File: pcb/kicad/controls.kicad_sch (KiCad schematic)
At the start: 0 parts

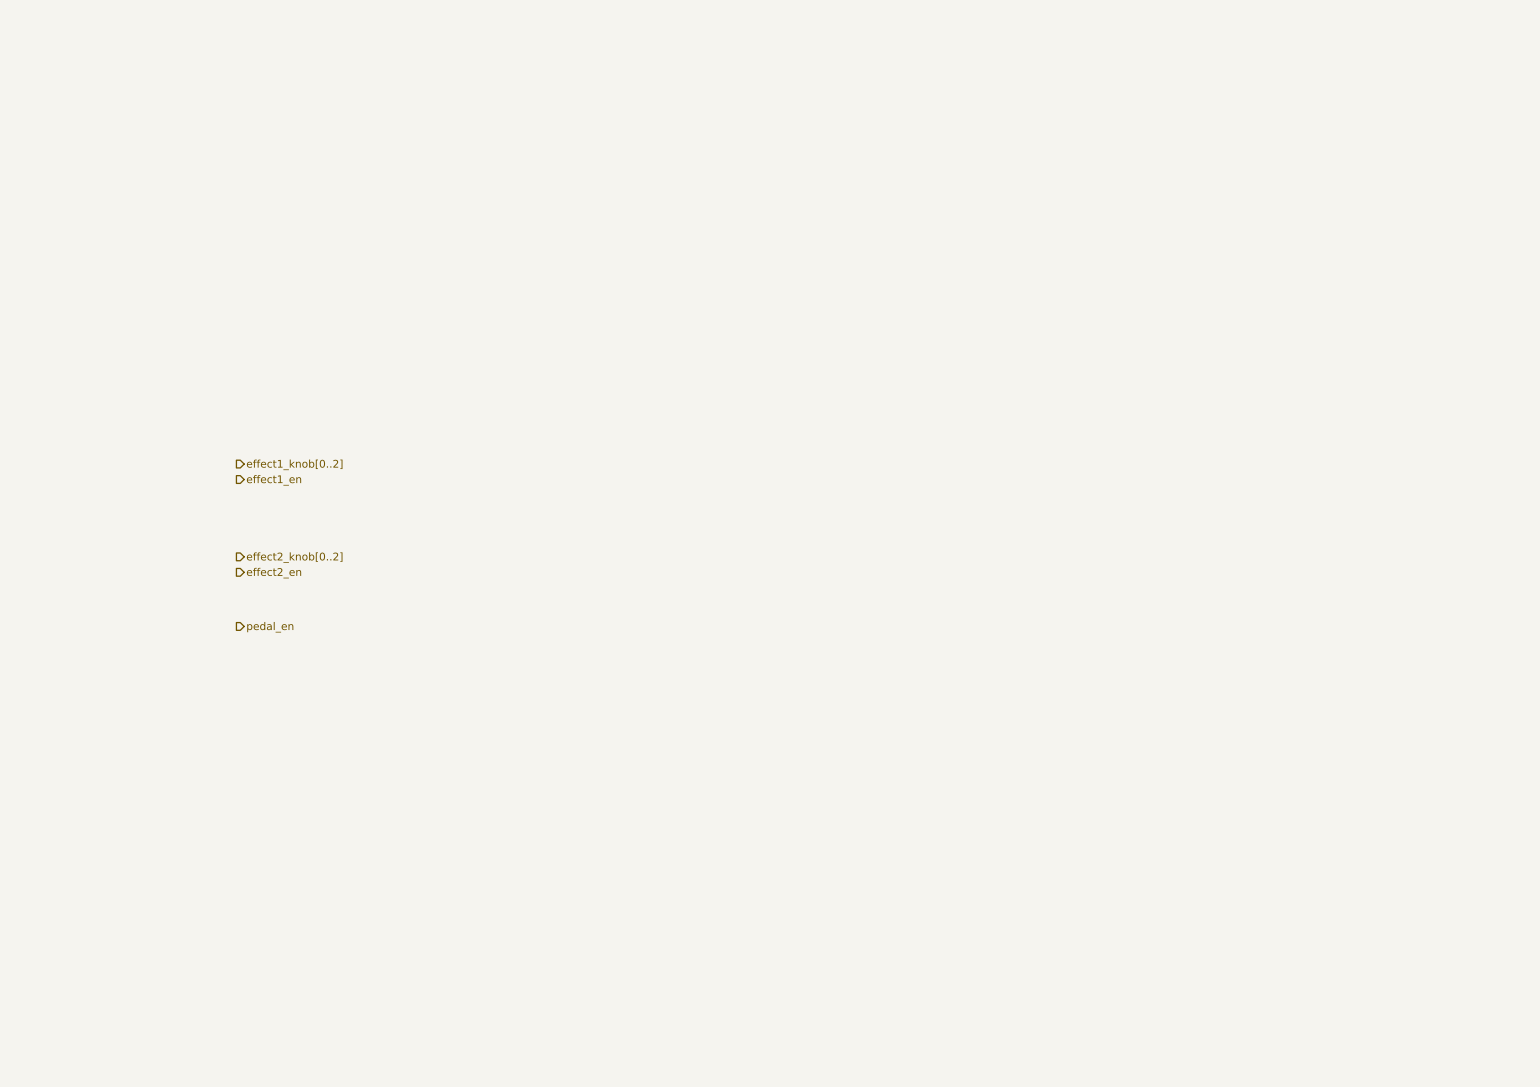
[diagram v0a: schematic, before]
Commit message: Added converters, controls and updated annotations.
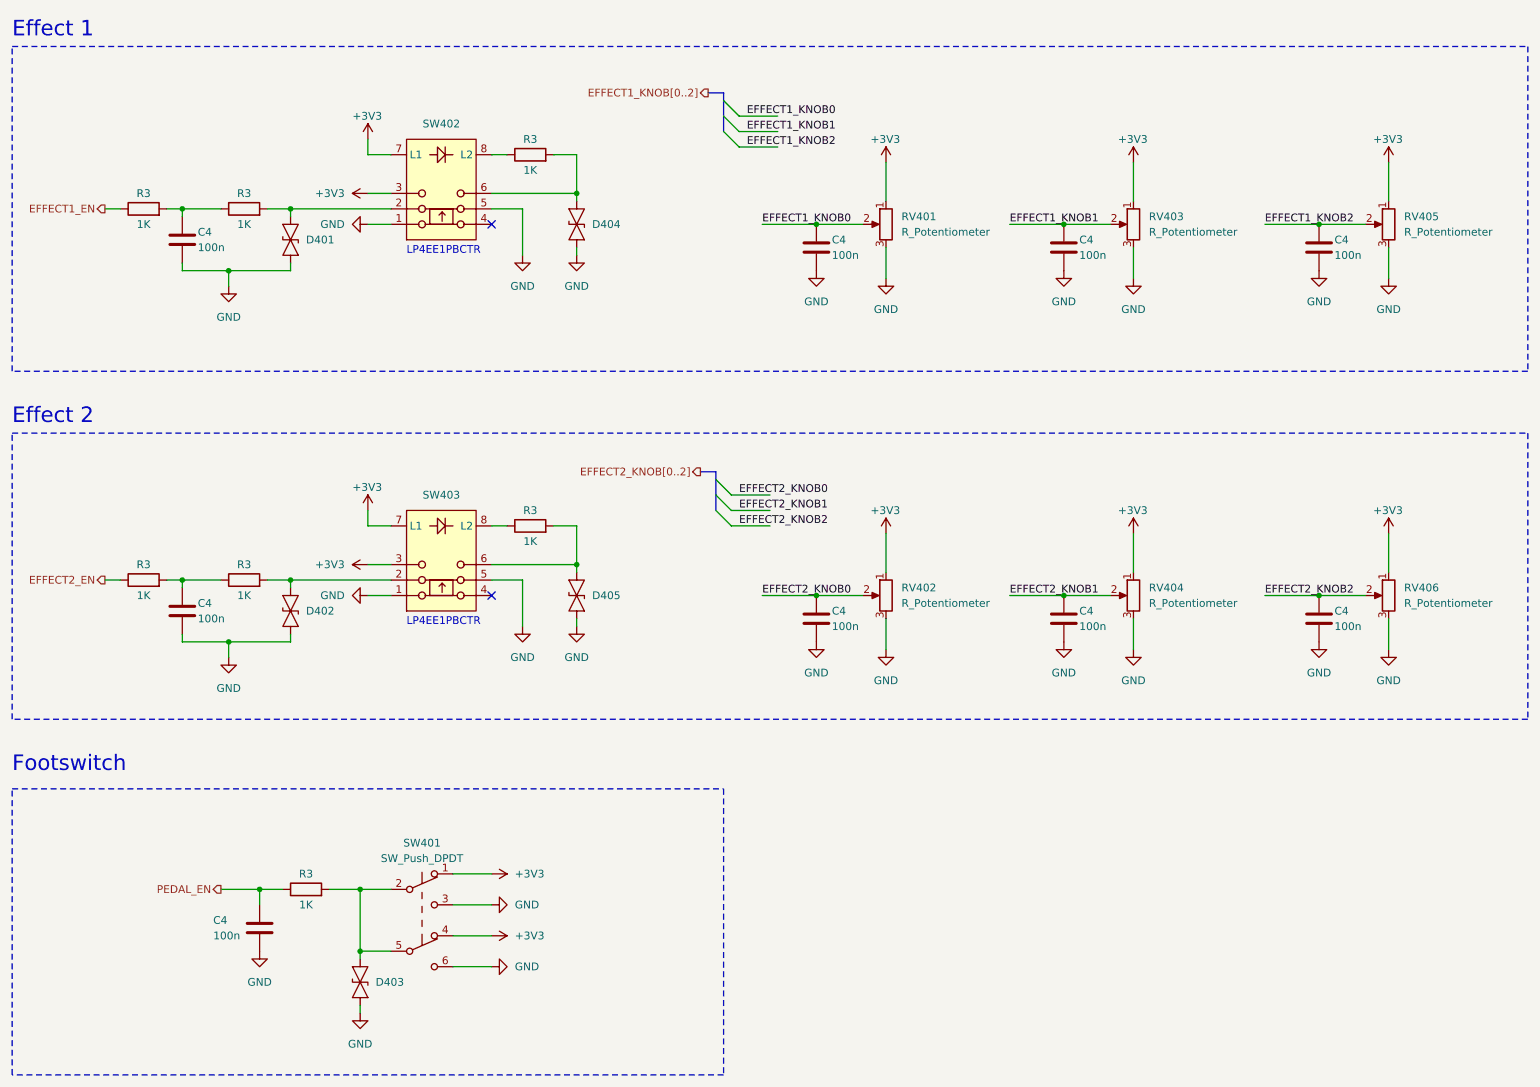
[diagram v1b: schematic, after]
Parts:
- added C4 (x9): 100n, Capacitor_SMD:C_0805_2012Metric, symbol Device:C
- added D401, D402, D403, D404, D405: ~, symbol pedal-components:PESD3V3L1BA
- added R3 (x7): 1K, Resistor_SMD:R_0805_2012Metric, symbol Device:R
- added RV401, RV402, RV403, RV404, RV405, RV406: R_Potentiometer, symbol Device:R_Potentiometer
- added SW401: SW_Push_DPDT, symbol Switch:SW_Push_DPDT
- added SW402, SW403: ~, symbol pedal-components:LP4EE1PBCTR
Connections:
- new net: D404.1 (A1), R3.2, SW402.6
- new net: C4.1, R3.1, R3.2 (x2)
- new net: D401.2 (A2), R3.2, SW402.2
- new net: R3.1, SW402.8 (L2)
- new net: D403.2 (A2), R3.2, SW401.2 (B), SW401.5 (B)
- new net: R3.1, SW403.8 (L2)
- new net: D405.1 (A1), R3.2, SW403.6
- new net: D402.2 (A2), R3.2, SW403.2
- new net +3V3: RV401.1, RV402.1, RV403.1, RV404.1, RV405.1, RV406.1, SW401.1 (A), SW401.4 (A), SW402.3, SW402.7 (L1), SW403.3, SW403.7 (L1)
- new net EFFECT1_EN: R3.1
- new net EFFECT1_KNOB0: C4.1, RV401.2
- new net EFFECT1_KNOB1: C4.1, RV403.2
- new net EFFECT1_KNOB2: C4.1, RV405.2
- new net EFFECT2_EN: R3.1
- new net EFFECT2_KNOB0: C4.1, RV402.2
- new net EFFECT2_KNOB1: C4.1, RV404.2
- new net EFFECT2_KNOB2: C4.1, RV406.2
- new net GND: C4.2, C4.2, C4.2, C4.2, C4.2, C4.2, C4.2, C4.2, C4.2, D401.1 (A1), D402.1 (A1), D403.1 (A1), D404.2 (A2), D405.2 (A2), RV401.3, RV402.3, RV403.3, RV404.3, RV405.3, RV406.3, SW401.3 (C), SW401.6 (C), SW402.1, SW402.5, SW403.1, SW403.5
- new net PEDAL_EN: C4.1, R3.1
- no-connect marks 0 -> 2
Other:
- note added: "Effect 1"
- note added: "Effect 2"
- note added: "Footswitch"
- note added: "LP4EE1PBCTR"

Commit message: Added PCB layout and fabrication output.
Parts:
- removed D401, D402, D403: ~, symbol pedal-components:PESD3V3L1BA
- added D301 (x3): ~, pedal-components:PESD3V3L1BA, symbol pedal-components:PESD3V3L1BA
- D404, D405: footprint (none) -> pedal-components:PESD3V3L1BA
- RV401, RV402, RV403, RV404, RV405, RV406: value R_Potentiometer -> 50K Linear; footprint (none) -> pedal-components:PTV09A-4030S-A503
- SW401: value SW_Push_DPDT -> PBS-24-202P; footprint (none) -> pedal-components:FSW-DPDT-020
- SW402, SW403: value ~ -> LP4EE1PBCTR; footprint (none) -> pedal-components:LP4EE1PBCTR
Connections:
- net EFFECT1_KNOB1: now also RV402.2; no longer RV403.2
- net EFFECT1_KNOB2: now also RV403.2; no longer RV405.2
- net EFFECT2_KNOB0: now also RV404.2; no longer RV402.2
- net EFFECT2_KNOB1: now also RV405.2; no longer RV404.2
- net GND: now also D301.1 (A1), D301.1 (A1), D301.1 (A1)
- net at R3.2, SW402.2: now also D301.2 (A2)
- net at R3.2, SW401.2 (B), SW401.5 (B): now also D301.2 (A2)
- net at R3.2, SW403.2: now also D301.2 (A2)
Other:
- note removed: "LP4EE1PBCTR"

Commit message: Add part numbers to components for ordering.
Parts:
- C4: Part Number (none) -> CC0805JRX7R9BB104
- D301, D404, D405: Part Number (none) -> PESD3V3L1BA,115
- R3: Part Number (none) -> RT0805FRE071KL
- RV401, RV402, RV403, RV404, RV405, RV406: Part Number (none) -> PTV09A-4030S-A503; Supplier Link (none) -> https://www.digikey.de/en/products/detail/bourns-inc/PTV09A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
- SW402, SW403: Part Number (none) -> LP4EE1PBCTR; Supplier Link (none) -> https://www.digikey.de/en/products/detail/e-switch/LP4EE1PB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
